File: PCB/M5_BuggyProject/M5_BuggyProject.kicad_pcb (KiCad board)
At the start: 2 copper layers, 40.6 x 90.2 mm, 26 parts, among them J1 XT60, J2 VCC, J3 10V

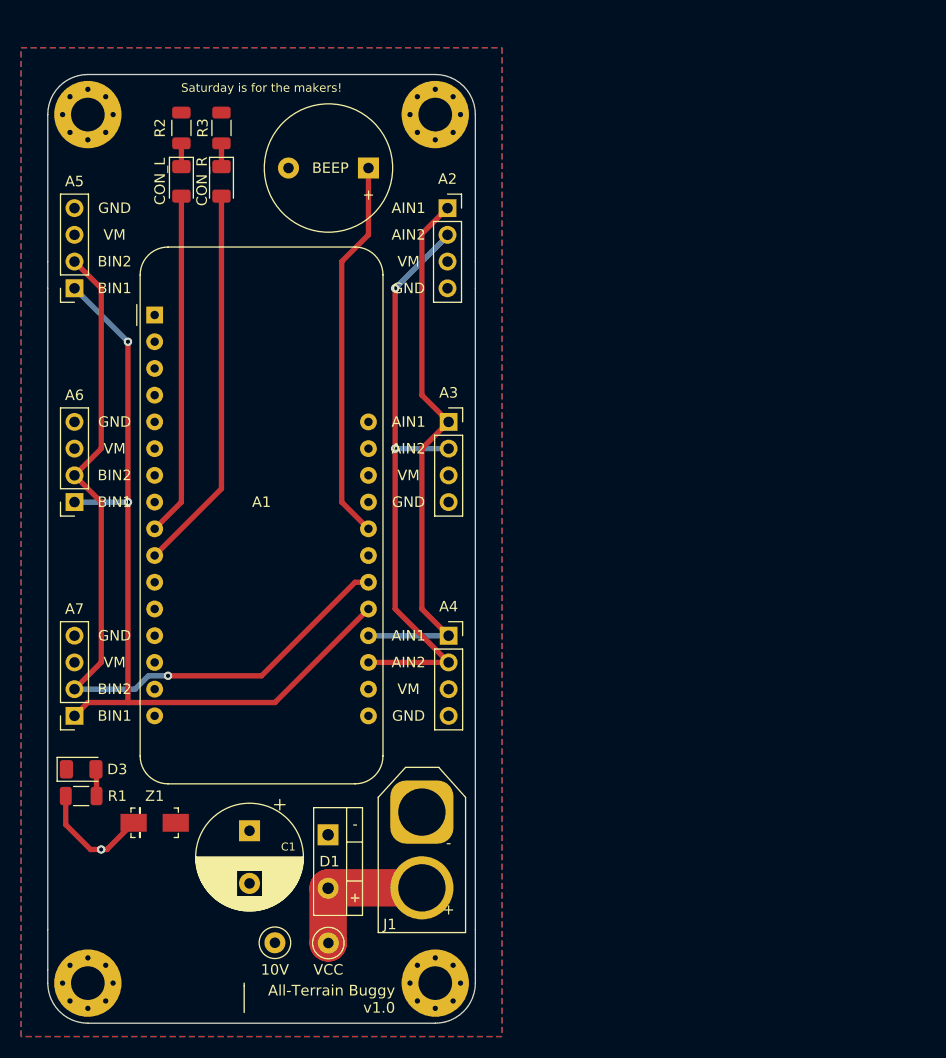
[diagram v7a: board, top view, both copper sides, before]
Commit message: Added connector for radio receiver
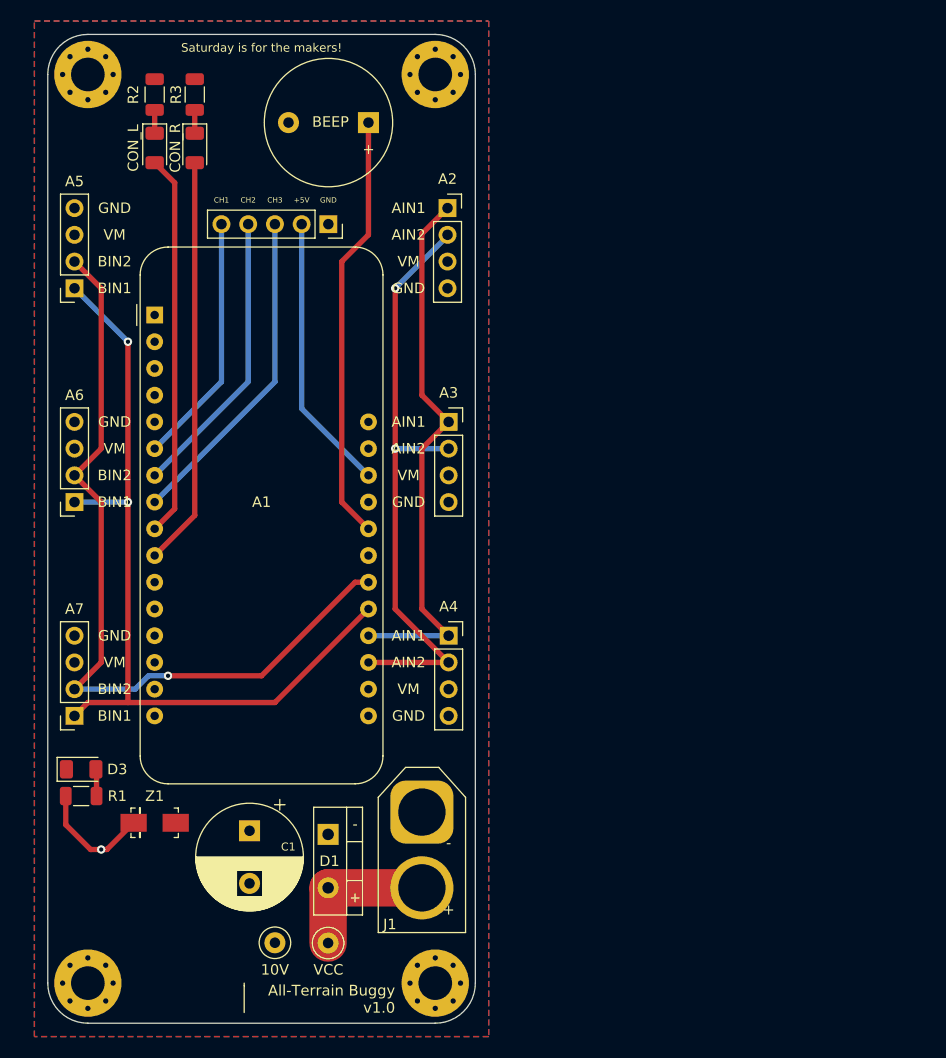
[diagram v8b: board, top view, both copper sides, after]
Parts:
- added J4: RF Receiver, Connector_PinSocket_2.54mm:PinSocket_1x05_P2.54mm_Vertical, F.Cu at (103.4, 49.5)
- moved BZ1 4.32 mm to (107.2, 39.9)
- moved D2 4.07 mm to (86.9, 42.3)
- moved D4 4.07 mm to (90.7, 42.3)
- moved R2 4.07 mm to (86.9, 37.2)
- moved R3 4.07 mm to (90.7, 37.2)
- moved H1 3.81 mm to (80.5, 35.3)
- moved H2 3.81 mm to (113.5, 35.3)
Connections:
- net Net-(A1-Pad2) renamed +3V3
- A1 pad 26: Net-(A1-Pad26) -> +5V
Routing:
- net CHANNEL_3: track 0.00 -> 31.2 mm
- net CHANNEL_2: track 0.00 -> 27.6 mm
- net +5V: track 0.00 -> 26.5 mm
- net CHANNEL_1: track 0.00 -> 24.0 mm
- net BEEP: track 36.4 -> 40.7 mm
- net CONFIG_L: track 32.7 -> 36.4 mm
- net CONFIG_R: track 36.8 -> 38.9 mm
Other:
- board size 40.6 x 90.2 mm -> 40.6 x 94 mm
- board text added: "+5V"
- board text added: "CH1"
- board text added: "CH2"
- board text added: "CH3"
